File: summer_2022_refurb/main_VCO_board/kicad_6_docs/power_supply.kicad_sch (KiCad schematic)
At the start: 0 parts

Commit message: Main VCO progress
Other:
- title: (none) -> Josh Ox Ribon Synth Main VCO board
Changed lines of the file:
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@@
 (kicad_sch (version 20211123) (generator eeschema)
   (paper "A4")
+  (title_block
+    (title "Josh Ox Ribon Synth Main VCO board")
+    (date "2022-06-18")
+    (rev "0")
+    (comment 2 "creativecommons.org/licences/by/4.0")
+    (comment 3 "license: CC by 4.0")
+    (comment 4 "Author: Jordan Acete")
+  )
 )

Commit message: Progress on main VCO, schem getting close but not done
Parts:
- added C2301, C2302, C2303, C2304, C2305, C2306, C2307, C2308, C2309, C2310, C2313, C2314, C2315, C2316, C2317, C2318, C2321, C2322, C2323, C2324, C2325, C2326, C2327, C2328, C2329, C2330, C2331, C2332, C2333, C2334, C2335, C2336, C2337, C2338, C2339, C2340, C2341, C2342: 100n, Capacitor_SMD:C_0805_2012Metric, symbol Device:C
- added C2311, C2312: 10u, Capacitor_THT:CP_Radial_D6.3mm_P2.50mm, symbol Device:C_Polarized
- added C2319, C2320: 330n, Capacitor_SMD:C_0805_2012Metric, symbol Device:C
- added J2301: power_entry, Connector_IDC:IDC-Header_2x05_P2.54mm_Vertical, symbol Connector_Generic:Conn_02x05_Odd_Even
- added R2301: 1k8, Resistor_SMD:R_0805_2012Metric, symbol Device:R
- added R2302: 4k7, Resistor_SMD:R_0805_2012Metric, symbol Device:R
- added R2303, R2304: 10k, Resistor_SMD:R_0805_2012Metric, symbol Device:R
- added TP2301: V+, TestPoint:TestPoint_Keystone_5000-5004_Miniature, symbol Connector:TestPoint
- added TP2302: V-, TestPoint:TestPoint_Keystone_5000-5004_Miniature, symbol Connector:TestPoint
- added TP2303: GND, TestPoint:TestPoint_Bridge_Pitch7.62mm_Drill1.3mm, symbol Connector:TestPoint
- added U1, U11, U12, U14, U15, U16, U2, U6, U8: TL074, symbol Amplifier_Operational:TL074
- added U10: DG413xY, Package_SO:SOIC-16_3.9x9.9mm_P1.27mm, symbol Analog_Switch:DG413xY
- added U17: NE5532, symbol Amplifier_Operational:NE5532
- added U18: TL072, Package_SO:SOIC-8_3.9x4.9mm_P1.27mm, symbol Amplifier_Operational:TL072
- added U2301: L78L05_SOT89, Package_TO_SOT_SMD:SOT-89-3, symbol Regulator_Linear:L78L05_SOT89
- added U2302: L79L05_SOT89, Package_TO_SOT_SMD:SOT-89-3, symbol Regulator_Linear:L79L05_SOT89
- added U2303: LM4040C-2.5, Package_TO_SOT_SMD:SOT-23, symbol Reference_Voltage:LM4040DBZ-2.5
- added U2304: LM4040DBZ-5, Package_TO_SOT_SMD:SOT-23, symbol Reference_Voltage:LM4040DBZ-5
- added U4: SSI2130, custom_footprints:PQN32_HandSoldering, symbol custom_symbols:SSI2130
- added U5: 4013, symbol 4xxx:4013
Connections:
- new net: C2338.2, R2303.1, R2304.2, U18.6 (-)
- new net +15V: C2301.1, C2303.1, C2305.1, C2307.1, C2309.1, C2311.1, C2313.1, C2315.1, C2317.1, C2319.1, C2321.1, C2323.1, C2327.1, J2301.10 (Pin_10), J2301.9 (Pin_9), R2302.1, TP2301.1, U1.4 (V+), U11.4 (V+), U12.4 (V+), U14.4 (V+), U15.4 (V+), U16.4 (V+), U17.8 (V+), U18.8 (V+), U2.4 (V+), U2301.3 (IN), U6.4 (V+), U8.4 (V+)
- new net +2V5 REF: C2329.1, R2301.2, U2303.1 (K)
- new net +5V: C2325.1, C2330.1, C2332.1, C2334.1, C2335.1, C2336.1, C2339.1, C2341.1, R2301.1, U10.12 (VL), U10.13 (V+), U2301.1 (OUT), U4.27 (V+), U5.14 (VDD)
- new net +5V REF: C2333.1, R2302.2, R2303.2, U2304.1 (K)
- new net -15V: C2302.2, C2304.2, C2306.2, C2308.2, C2310.2, C2312.2, C2314.2, C2316.2, C2318.2, C2320.2, C2322.2, C2324.2, C2328.2, J2301.1 (Pin_1), J2301.2 (Pin_2), TP2302.1, U1.11 (V-), U11.11 (V-), U12.11 (V-), U14.11 (V-), U15.11 (V-), U16.11 (V-), U17.4 (V-), U18.4 (V-), U2.11 (V-), U2302.2 (VI), U6.11 (V-), U8.11 (V-)
- new net -5V: C2326.2, C2331.2, C2337.2, C2340.2, C2342.2, U10.4 (V-), U2302.3 (VO), U4.8 (V-)
- new net -5V REF: C2338.1, R2304.1, U18.7
- new net GND: C2301.2, C2302.1, C2303.2, C2304.1, C2305.2, C2306.1, C2307.2, C2308.1, C2309.2, C2310.1, C2311.2, C2312.1, C2313.2, C2314.1, C2315.2, C2316.1, C2317.2, C2318.1, C2319.2, C2320.1, C2321.2, C2322.1, C2323.2, C2324.1, C2325.2, C2326.1, C2327.2, C2328.1, C2329.2, C2330.2, C2331.1, C2332.2, C2333.2, C2334.2, C2335.2, C2336.2, C2337.1, C2339.2, C2340.1, C2341.2, C2342.1, J2301.3 (Pin_3), J2301.4 (Pin_4), J2301.5 (Pin_5), J2301.6 (Pin_6), J2301.7 (Pin_7), J2301.8 (Pin_8), TP2303.1, U10.5 (GND), U18.5 (+), U2301.2 (GND), U2302.1 (GND), U2303.2 (A), U2304.2 (A), U4.15 (dgnd), U4.16 (agnd), U5.7 (VSS)
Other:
- note added: "Bulk Decoupling"
- note added: "Logic Decoupling"
- note added: "Logic Power"
- note added: "Opamp Decoupling"
- note added: "Opamp Power"

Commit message: Main VCO rough parts placement
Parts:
- U1, U11, U12, U14, U15, U16, U2, U5, U6, U8: footprint (none) -> Package_SO:SOIC-14_3.9x8.7mm_P1.27mm
- U17: footprint (none) -> Package_SO:SOIC-8_3.9x4.9mm_P1.27mm
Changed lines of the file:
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@@
       (effects (font (size 1.27 1.27)) (justify left))
     )
-    (property "Footprint" "" (id 2) (at 124.46 46.99 0)
+    (property "Footprint" "Package_SO:SOIC-14_3.9x8.7mm_P1.27mm" (id 2) (at 124.46 46.99 0)
       (effects (font (size 1.27 1.27)) hide)
     )
@@
       (effects (font (size 1.27 1.27)) (justify left))
     )
-    (property "Footprint" "" (id 2) (at 99.06 46.99 0)
+    (property "Footprint" "Package_SO:SOIC-14_3.9x8.7mm_P1.27mm" (id 2) (at 99.06 46.99 0)
       (effects (font (size 1.27 1.27)) hide)
     )
@@
       (effects (font (size 1.27 1.27)) (justify left))
     )
-    (property "Footprint" "" (id 2) (at 73.66 46.99 0)
+    (property "Footprint" "Package_SO:SOIC-14_3.9x8.7mm_P1.27mm" (id 2) (at 73.66 46.99 0)
       (effects (font (size 1.27 1.27)) hide)
     )
@@
       (effects (font (size 1.27 1.27)) (justify left))
     )
-    (property "Footprint" "" (id 2) (at 229.87 50.8 0)
+    (property "Footprint" "Package_SO:SOIC-14_3.9x8.7mm_P1.27mm" (id 2) (at 229.87 50.8 0)
       (effects (font (size 1.27 1.27)) hide)
     )
@@
       (effects (font (size 1.27 1.27)) (justify left))
     )
-    (property "Footprint" "" (id 2) (at 86.36 46.99 0)
+    (property "Footprint" "Package_SO:SOIC-14_3.9x8.7mm_P1.27mm" (id 2) (at 86.36 46.99 0)
       (effects (font (size 1.27 1.27)) hide)
     )
@@
       (effects (font (size 1.27 1.27)) (justify left))
     )
-    (property "Footprint" "" (id 2) (at 137.16 46.99 0)
+    (property "Footprint" "Package_SO:SOIC-14_3.9x8.7mm_P1.27mm" (id 2) (at 137.16 46.99 0)
       (effects (font (size 1.27 1.27)) hide)
     )
@@
       (effects (font (size 1.27 1.27)) (justify left))
     )
-    (property "Footprint" "" (id 2) (at 48.26 46.99 0)
+    (property "Footprint" "Package_SO:SOIC-14_3.9x8.7mm_P1.27mm" (id 2) (at 48.26 46.99 0)
       (effects (font (size 1.27 1.27)) hide)
     )
@@
       (effects (font (size 1.27 1.27)) (justify left))
     )
-    (property "Footprint" "" (id 2) (at 60.96 46.99 0)
+    (property "Footprint" "Package_SO:SOIC-14_3.9x8.7mm_P1.27mm" (id 2) (at 60.96 46.99 0)
       (effects (font (size 1.27 1.27)) hide)
     )
@@
       (effects (font (size 1.27 1.27)) (justify left))
     )
-    (property "Footprint" "" (id 2) (at 35.56 46.99 0)
+    (property "Footprint" "Package_SO:SOIC-14_3.9x8.7mm_P1.27mm" (id 2) (at 35.56 46.99 0)
       (effects (font (size 1.27 1.27)) hide)
     )
@@
       (effects (font (size 1.27 1.27)) (justify left))
     )
-    (property "Footprint" "" (id 2) (at 151.13 49.53 0)
+    (property "Footprint" "Package_SO:SOIC-8_3.9x4.9mm_P1.27mm" (id 2) (at 151.13 49.53 0)
       (effects (font (size 1.27 1.27)) hide)
     )
@@
       (effects (font (size 1.27 1.27)) (justify left))
     )
-    (property "Footprint" "" (id 2) (at 111.76 46.99 0)
-      (effects (font (size 1.27 1.27)) hide)
-    )
+    (property "Footprint" "Package_SO:SOIC-14_3.9x8.7mm_P1.27mm" (id 2) (at 111.76 46.99 0)
+      (effects (font (size 1.27 1.27)) hide)
+    )

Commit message: Begin VCO pcb layout
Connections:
- net +15V: now also C2336.1, C2341.1, U10.13 (V+)
- net +5V: no longer C2336.1, C2341.1, U10.13 (V+)
- net -15V: now also C2337.2, U10.4 (V-)
- net -5V: no longer C2337.2, U10.4 (V-)
- net +2V5 REF renamed +2V5_REF
- net +5V REF renamed +5V_REF
- net -5V REF renamed -5V_REF
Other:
- moved on the sheet: C2330, C2331, C2336, C2337, C2341

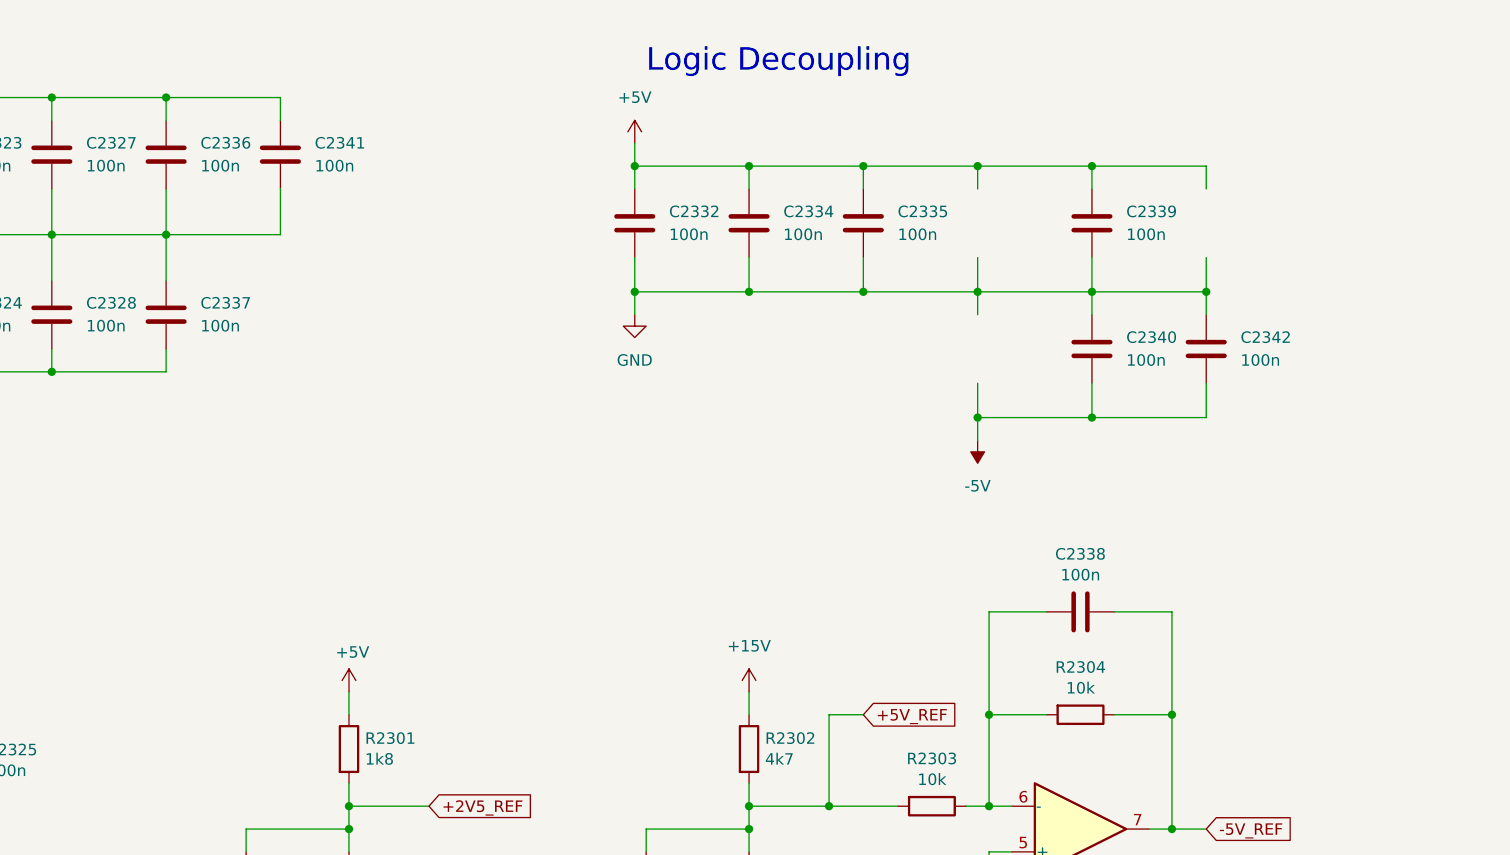
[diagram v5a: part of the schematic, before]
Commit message: Initial VCO layout
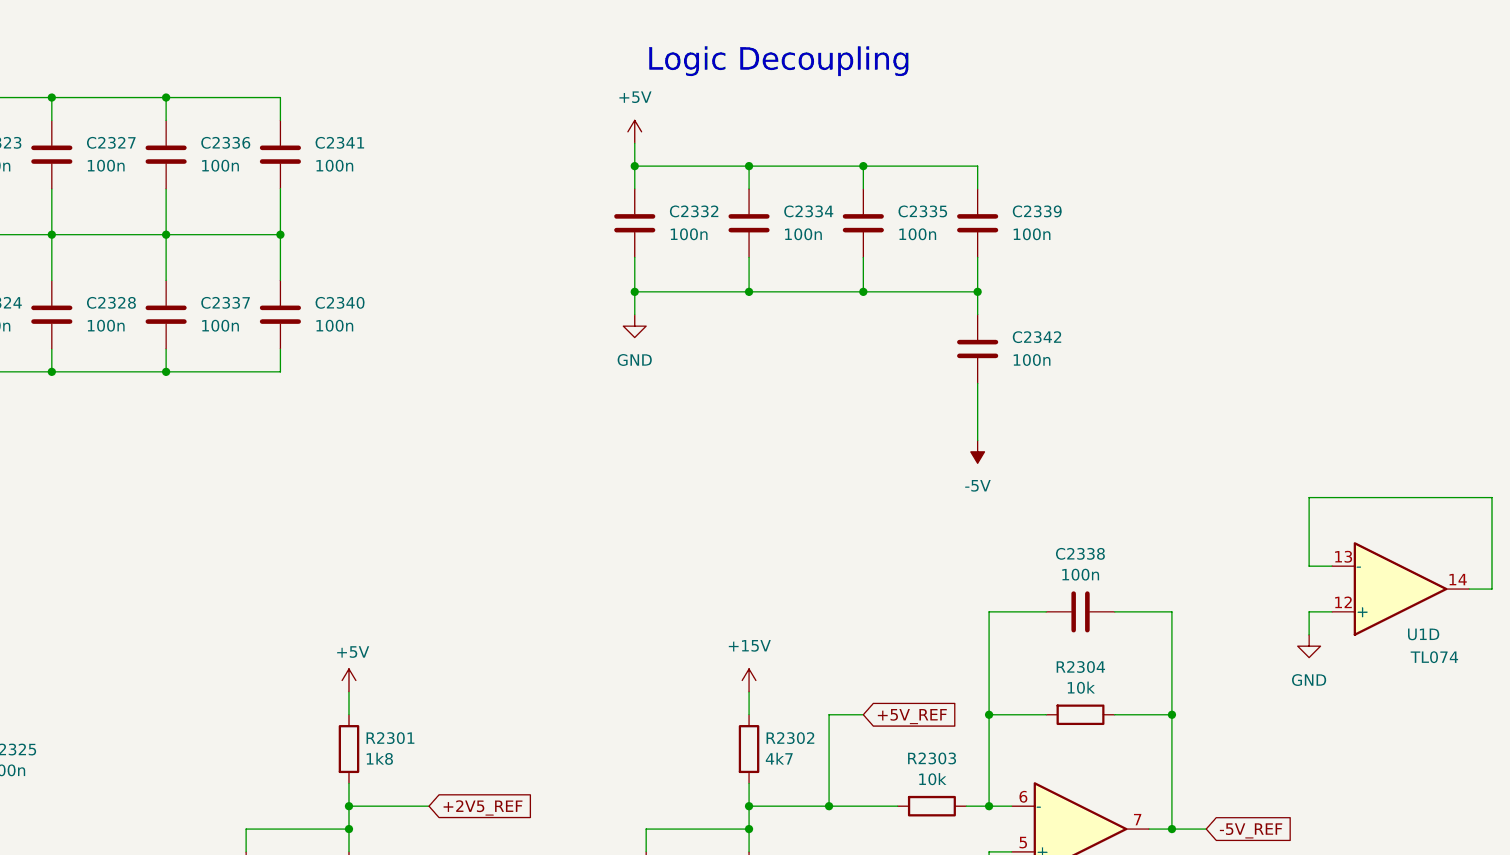
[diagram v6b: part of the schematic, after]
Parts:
- added unit 4 of U1
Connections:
- net -15V: now also C2340.2
- net -5V: no longer C2340.2
- net GND: now also U1.12 (+)
- new net: U1.13 (-), U1.14
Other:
- moved on the sheet: C2339, C2340, C2342
